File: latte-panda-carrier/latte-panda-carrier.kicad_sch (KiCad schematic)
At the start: 6 parts

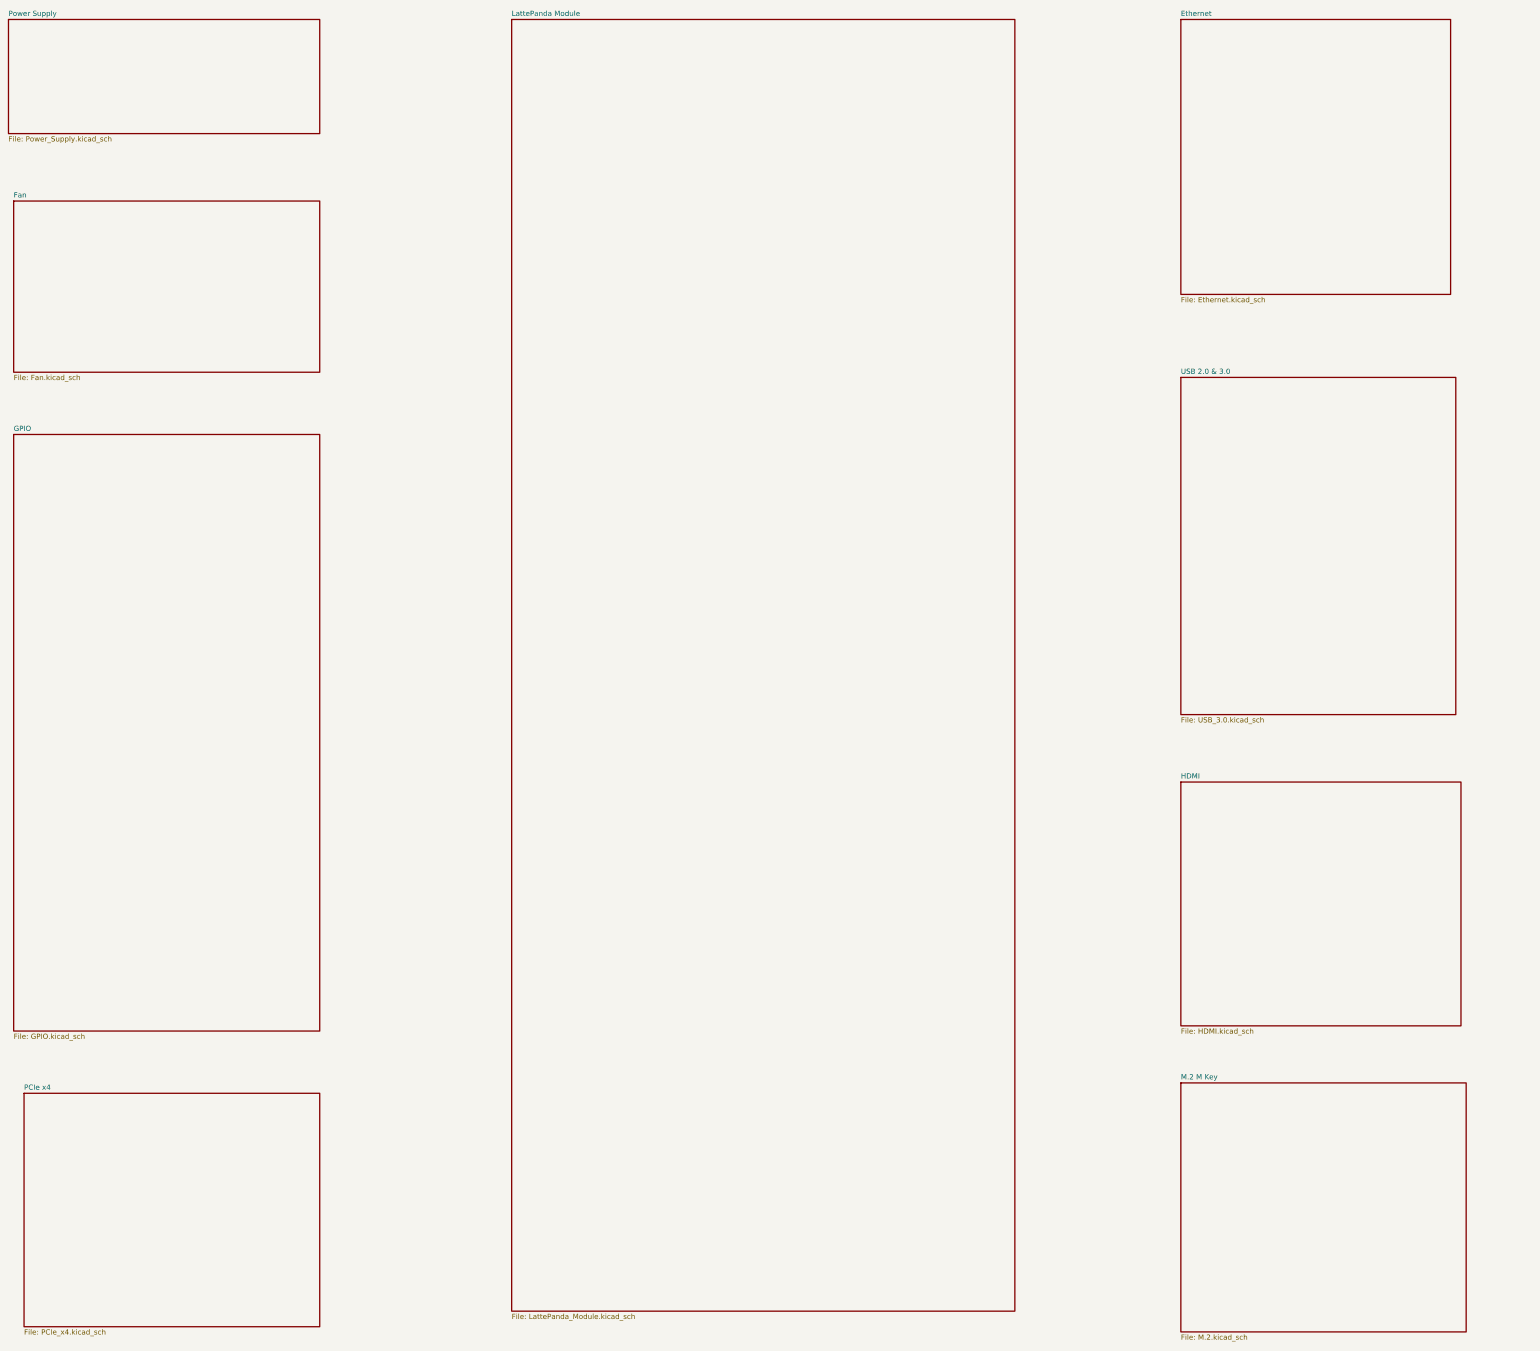
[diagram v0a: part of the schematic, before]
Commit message: 100.4
Add LattePanda Mu -schematic pins.
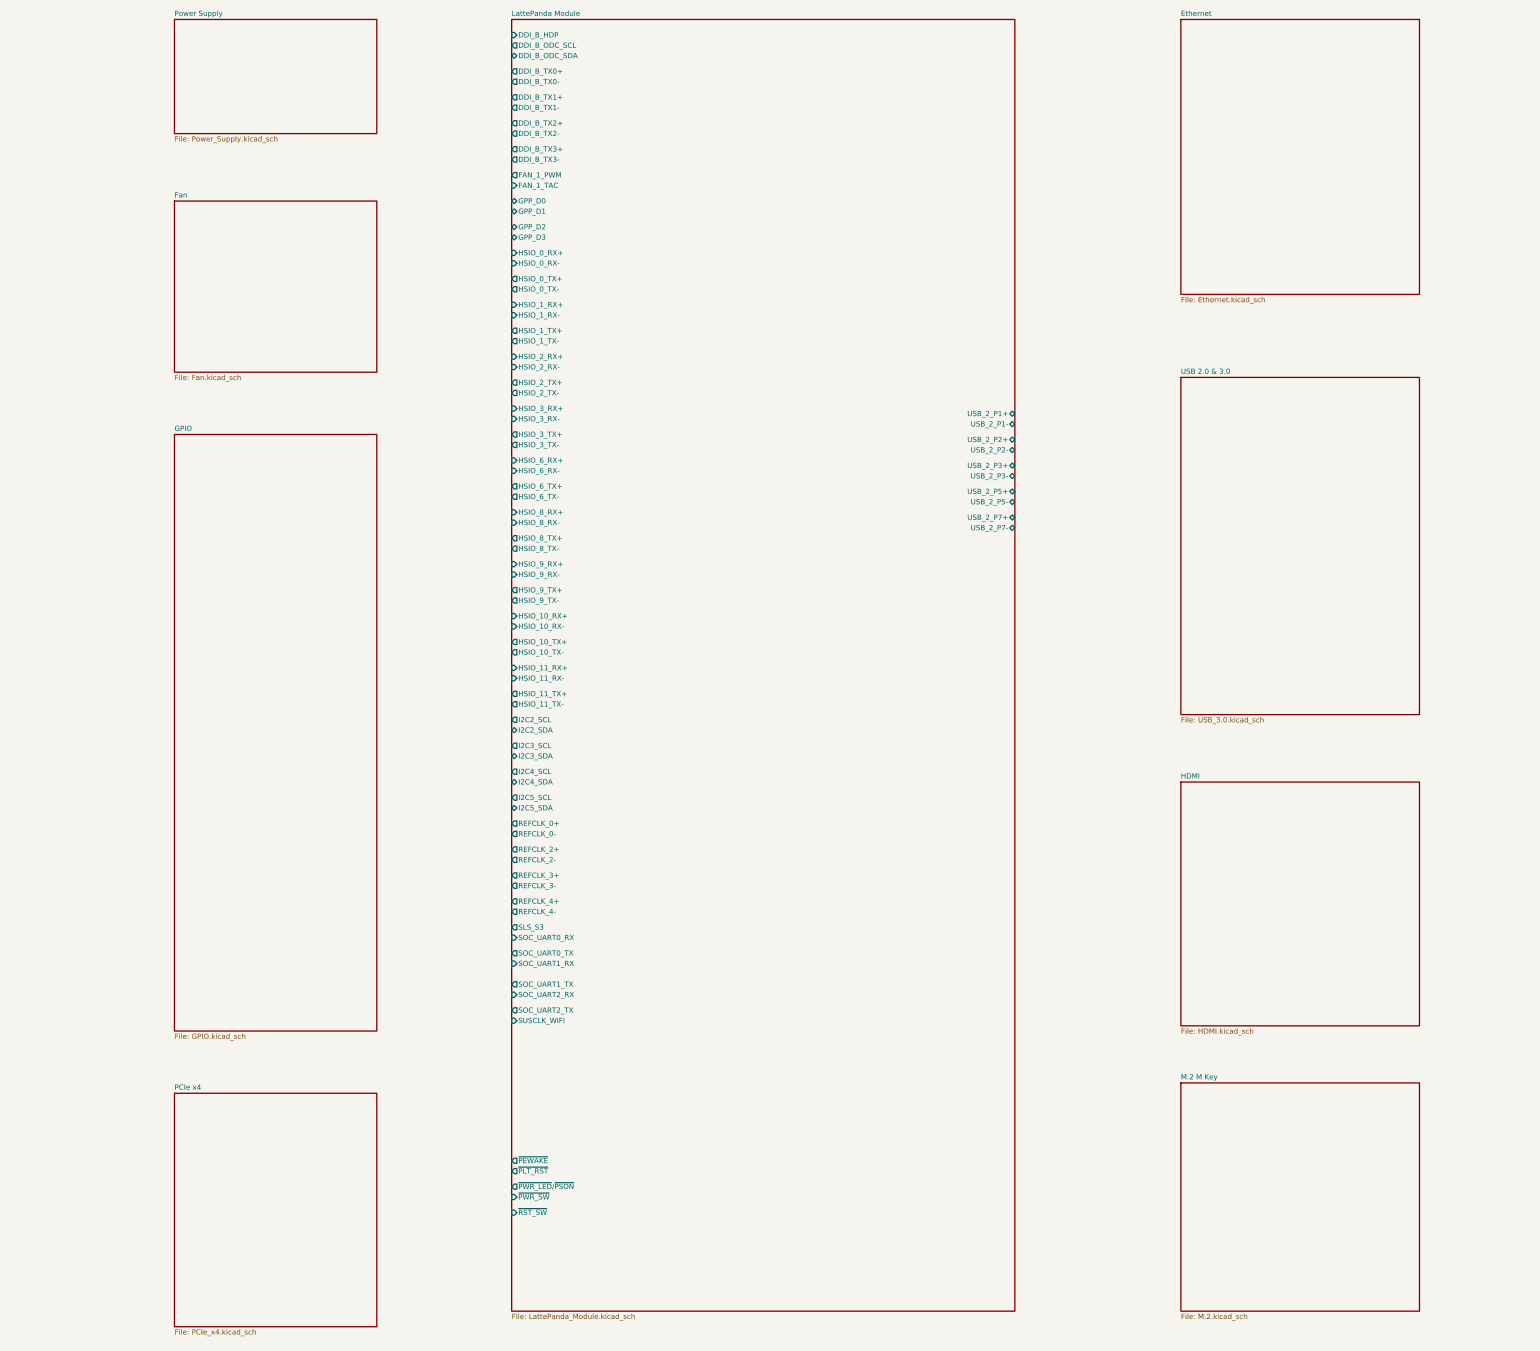
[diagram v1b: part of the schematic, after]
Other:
- sheet LattePanda Module ports: added DDI_B_HDP, DDI_B_ODC_SCL, DDI_B_ODC_SDA, DDI_B_TX0+, DDI_B_TX0-, DDI_B_TX1+, DDI_B_TX1-, DDI_B_TX2+, DDI_B_TX2-, DDI_B_TX3+, DDI_B_TX3-, FAN_1_PWM, FAN_1_TAC, GPP_D0, GPP_D1, GPP_D2, GPP_D3, HSIO_0_RX+, HSIO_0_RX-, HSIO_0_TX+, HSIO_0_TX-, HSIO_10_RX+, HSIO_10_RX-, HSIO_10_TX+, HSIO_10_TX-, HSIO_11_RX+, HSIO_11_RX-, HSIO_11_TX+, HSIO_11_TX-, HSIO_1_RX+, HSIO_1_RX-, HSIO_1_TX+, HSIO_1_TX-, HSIO_2_RX+, HSIO_2_RX-, HSIO_2_TX+, HSIO_2_TX-, HSIO_3_RX+, HSIO_3_RX-, HSIO_3_TX+, HSIO_3_TX-, HSIO_6_RX+, HSIO_6_RX-, HSIO_6_TX+, HSIO_6_TX-, HSIO_8_RX+, HSIO_8_RX-, HSIO_8_TX+, HSIO_8_TX-, HSIO_9_RX+, HSIO_9_RX-, HSIO_9_TX+, HSIO_9_TX-, I2C2_SCL, I2C2_SDA, I2C3_SCL, I2C3_SDA, I2C4_SCL, I2C4_SDA, I2C5_SCL, I2C5_SDA, REFCLK_0+, REFCLK_0-, REFCLK_2+, REFCLK_2-, REFCLK_3+, REFCLK_3-, REFCLK_4+, REFCLK_4-, SLS_S3, SOC_UART0_RX, SOC_UART0_TX, SOC_UART1_RX, SOC_UART1_TX, SOC_UART2_RX, SOC_UART2_TX, SUSCLK_WIFI, USB_2_P1+, USB_2_P1-, USB_2_P2+, USB_2_P2-, USB_2_P3+, USB_2_P3-, USB_2_P5+, USB_2_P5-, USB_2_P7+, USB_2_P7-, ~{PEWAKE}, ~{PLT_RST}, ~{PWR_LED}/~{PSON}, ~{PWR_SW}, ~{RST_SW}; removed none

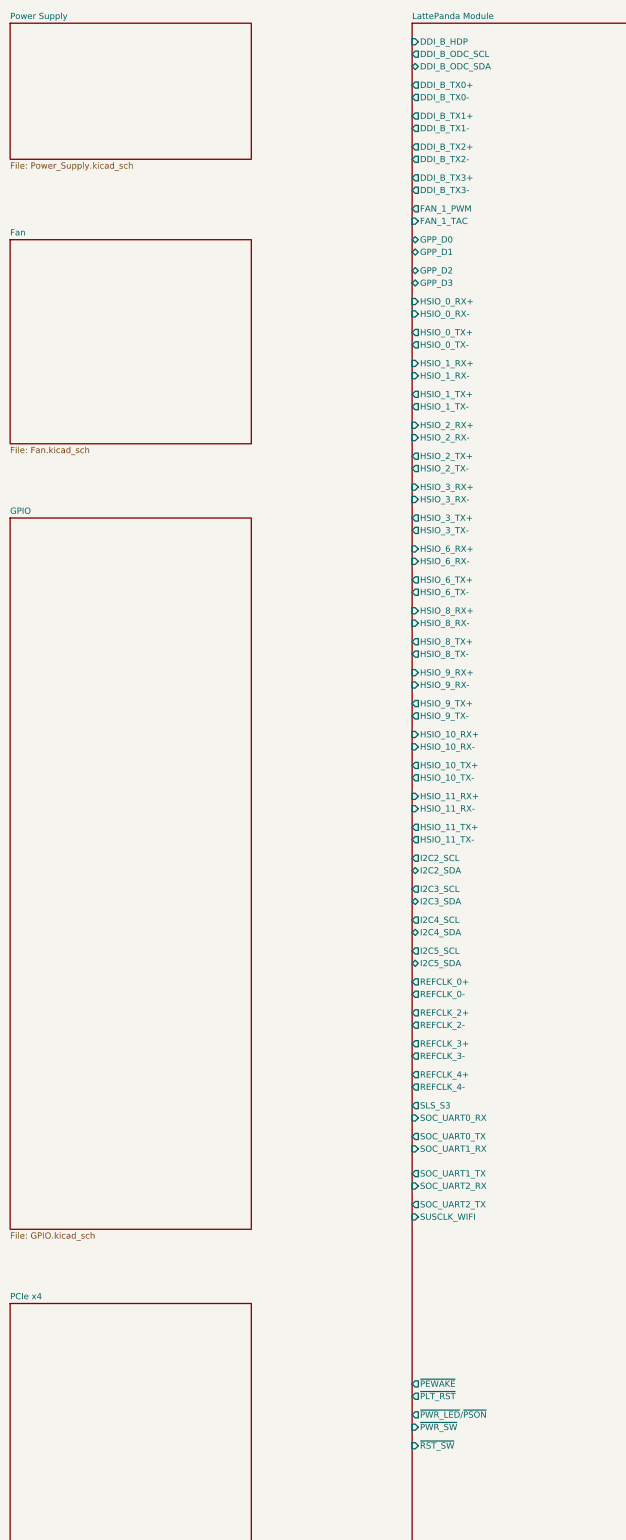
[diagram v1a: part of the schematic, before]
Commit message: Connected sheet pins for PSU through root sheet
Changed not connected pin errors to warnings and also cleared rest of the
errors.
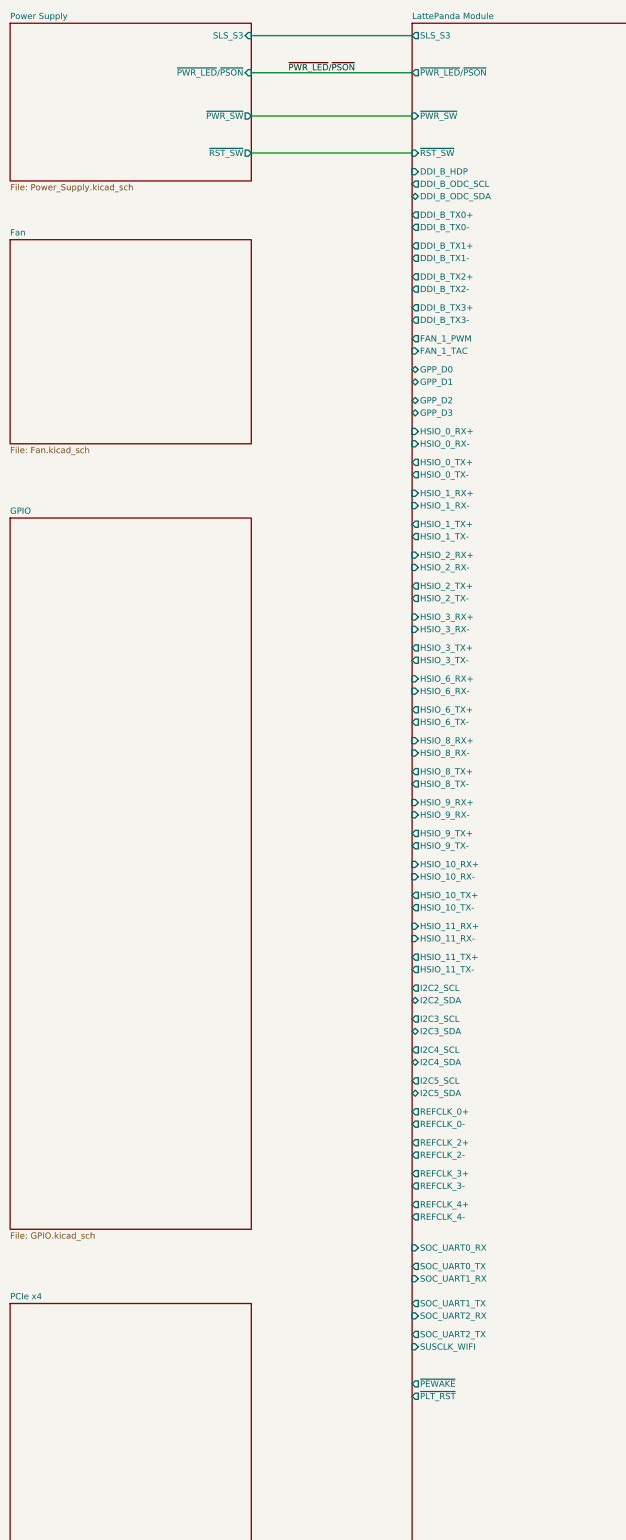
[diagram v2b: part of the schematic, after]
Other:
- sheet Power Supply ports: added SLS_S3, ~{PWR_LED}/~{PSON}, ~{PWR_SW}, ~{RST_SW}; removed none
